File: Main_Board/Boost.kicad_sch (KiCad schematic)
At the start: 13 parts, among them U5 TLV61070ADBV

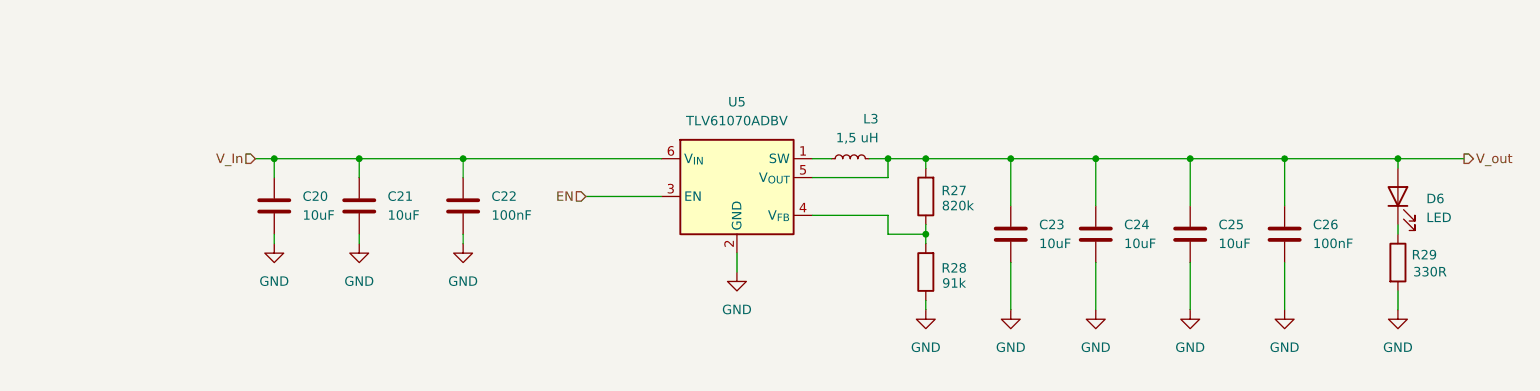
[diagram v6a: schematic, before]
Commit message: Fix boost schematic +layout
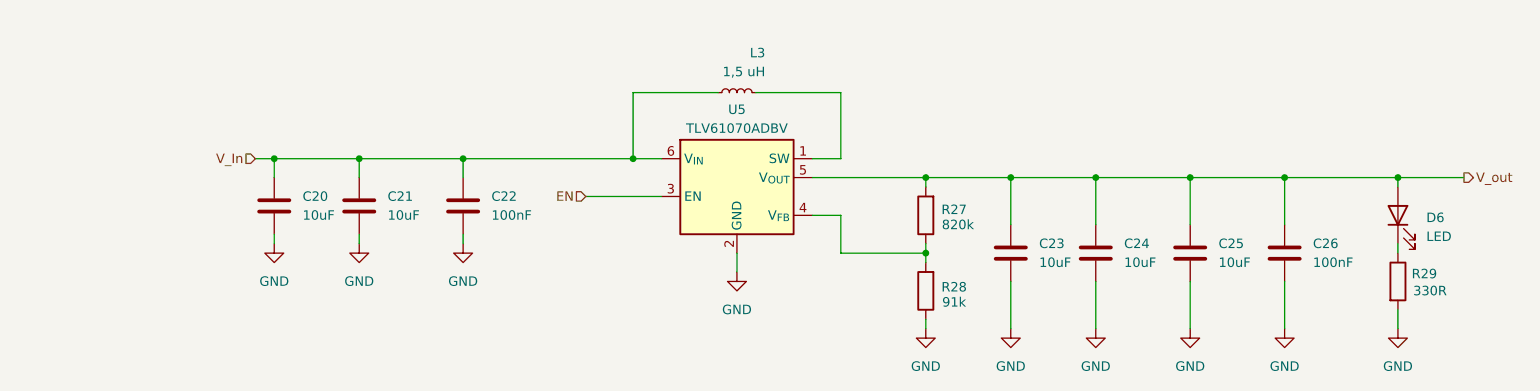
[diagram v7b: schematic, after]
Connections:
- net V_In: now also L3.2
- net V_out: no longer L3.1
- net at U5.1 (SW): now also L3.1; no longer L3.2
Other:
- moved on the sheet: C23, C24, C25, C26, D6, L3, R27, R28, R29

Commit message: New boost inductor (needs to be verified)
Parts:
- L3: value 1,5 uH -> 4,7uH; footprint Inductor_SMD:L_Taiyo-Yuden_MD-3030 -> Inductor_SMD:L_1210_3225Metric
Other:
- note added: "Inductor: Murata DFE322520FD-2R2M=P2"
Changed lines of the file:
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@@
 	(generator_version "10.0")
 	(paper "A4")
+	(text "Inductor: Murata DFE322520FD-2R2M=P2"
+		(exclude_from_sim no)
+		(at 134.112 74.93 0)
+		(effects
+			(font
+				(size 1.27 1.27)
+			)
+		)
+	)
 	(junction
 		(at 222.25 95.25)
@@
 			)
 		)
-		(property "Value" "1,5 uH"
+		(property "Value" "4,7uH"
 			(at 137.16 81.026 90)
 			(show_name no)
@@
 			)
 		)
-		(property "Footprint" "Inductor_SMD:L_Taiyo-Yuden_MD-3030"
+		(property "Footprint" "Inductor_SMD:L_1210_3225Metric"
 			(at 133.35 83.82 0)
 			(hide yes)
